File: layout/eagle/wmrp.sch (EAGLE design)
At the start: 131 parts, among them IC1 ACS712, IC2 ADR392, IC3 ATMEGA32U4TQFP-44, IC4 AD8552, IC5 AD8552, Q1 BC817-40, Q2 BC817-40, Q3 IRF7416, Q4 IRF7413, Q5 BC817-40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

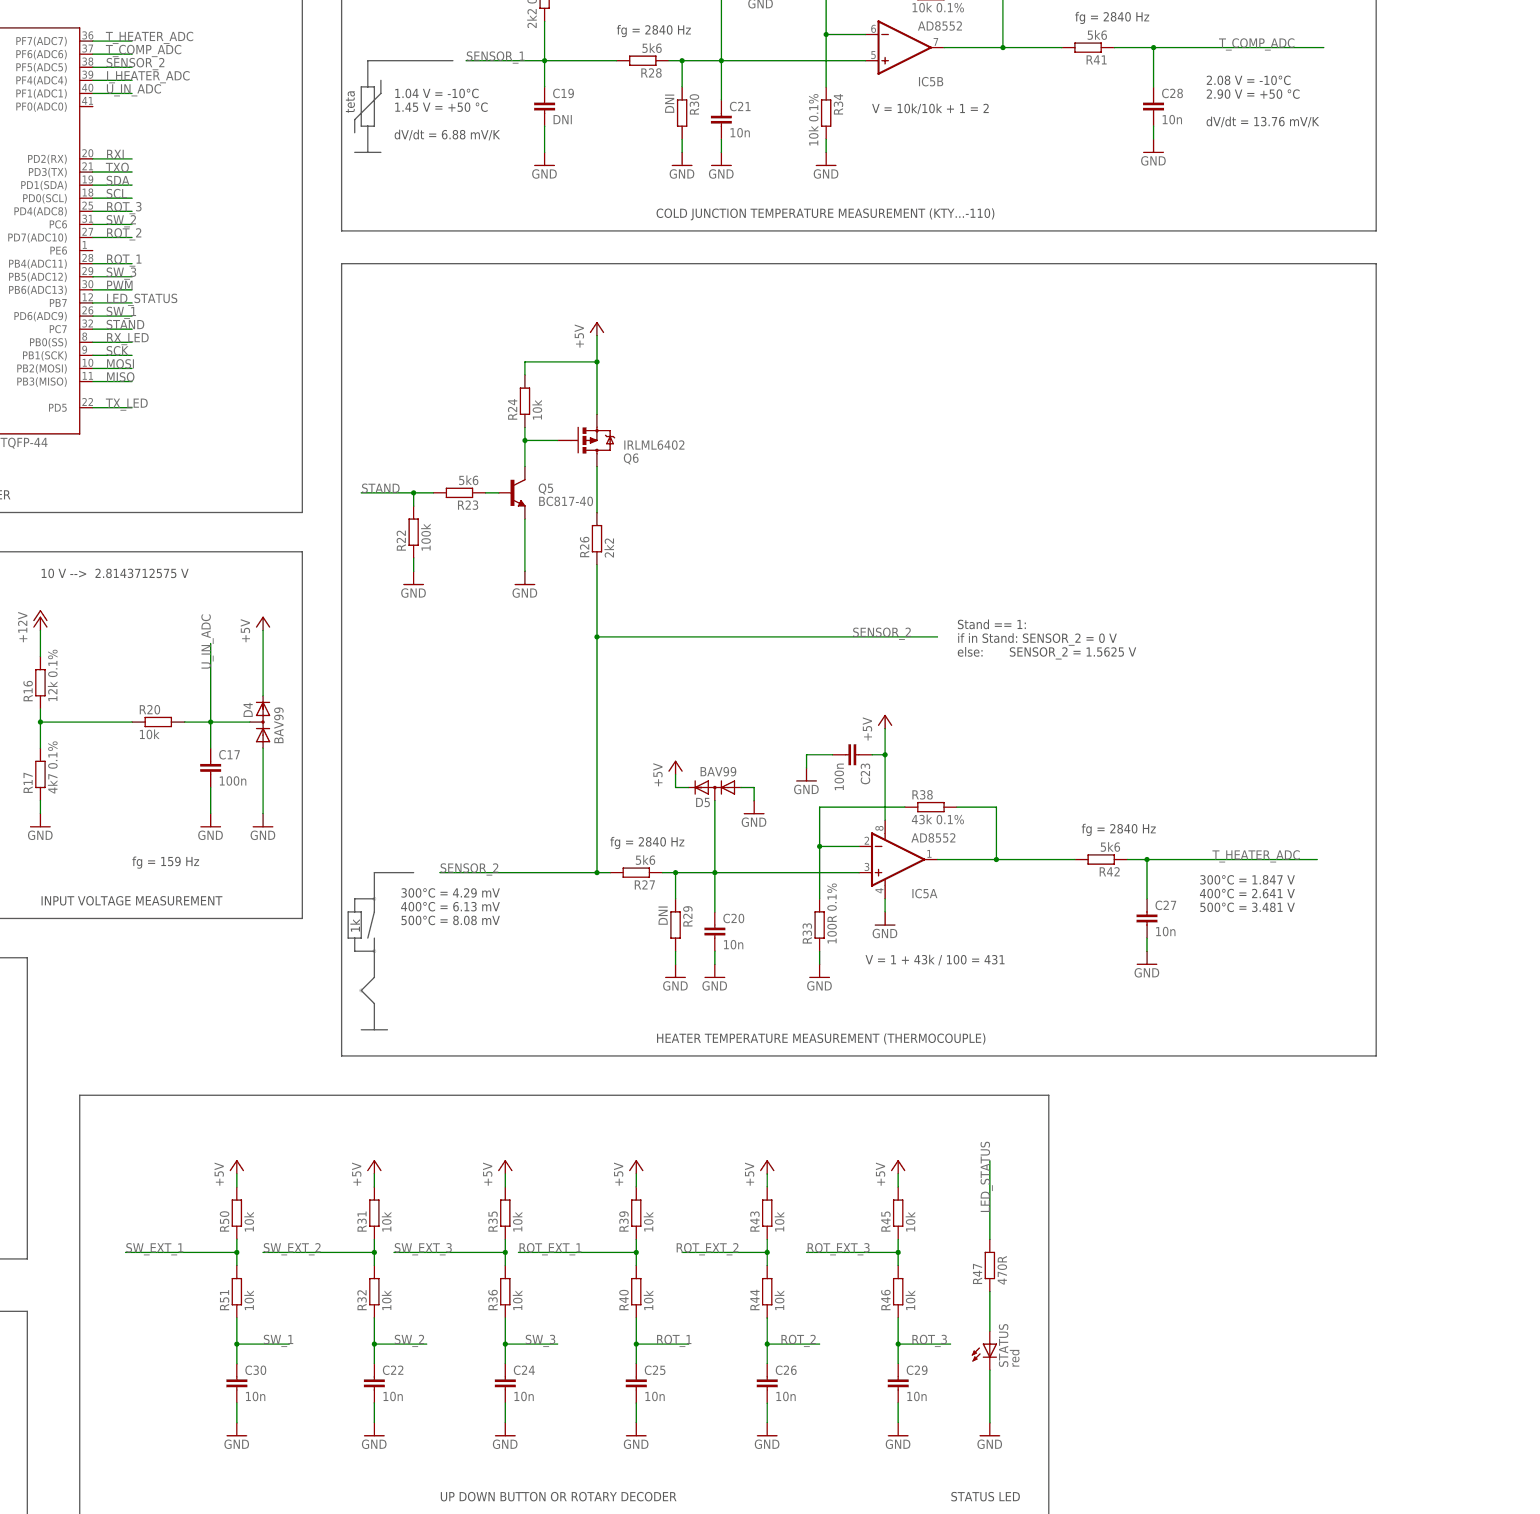
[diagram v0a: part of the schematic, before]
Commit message: Added SPI header and resistors to schematic, added SC and BL pin, moved RX_LED from pin 8 to 1
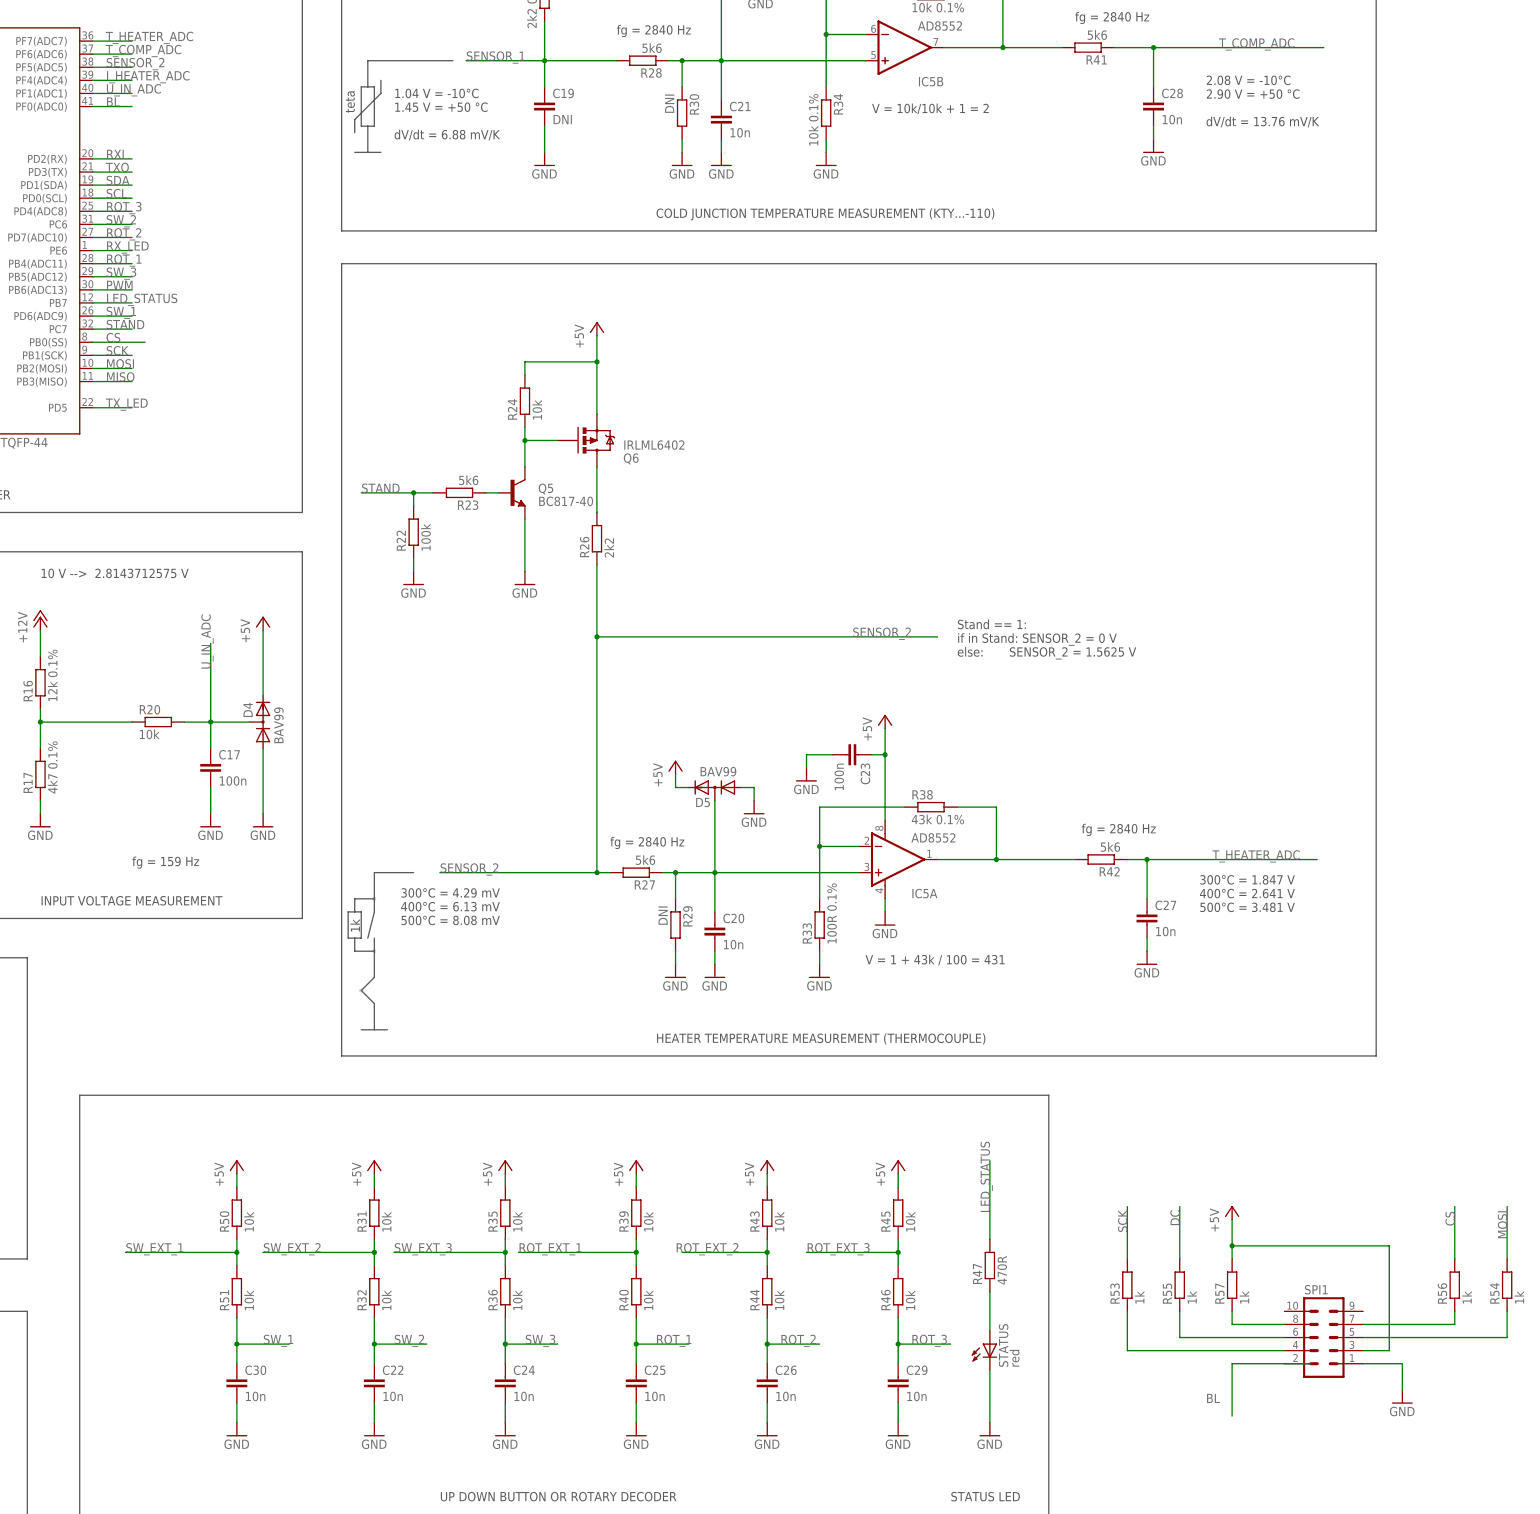
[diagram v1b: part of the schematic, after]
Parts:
- added R53, R54, R55, R56, R57: 1k, resistor:R-EU_R1206
- added SPI1: (no value), con-lstb:MA05-2
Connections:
- new net BL: IC3.PF0(ADC0), SPI1.2
- new net CS: IC3.PB0(SS), R56.2
- new net DC: R55.2
- new net N$35: R53.1, SPI1.4
- new net N$36: R54.1, SPI1.5
- new net N$37: R55.1, SPI1.6
- new net N$38: R56.1, SPI1.7
- new net N$40: R57.1, SPI1.8
- net +5V: now also R57.2, SPI1.3
- net GND: now also SPI1.1
- net MOSI: now also R54.2
- net RX_LED: now also IC3.PE6; no longer IC3.PB0(SS)
- net SCK: now also R53.2
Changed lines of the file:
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@@
 <?xml version="1.0" encoding="utf-8"?>
 <!DOCTYPE eagle SYSTEM "eagle.dtd">
-<eagle version="7.1.0">
+<eagle version="7.7.0">
 <drawing>
 <settings>
@@
 <setting verticaltext="up"/>
 </settings>
-<grid distance="0.1" unitdist="inch" unit="inch" style="lines" multiple="1" display="no" altdistance="0.01" altunitdist="inch" altunit="inch"/>
+<grid distance="0.1" unitdist="inch" unit="inch" style="lines" multiple="1" display="yes" altdistance="0.01" altunitdist="inch" altunit="inch"/>
 <layers>
 <layer number="1" name="Top" color="4" fill="1" visible="no" active="no"/>
@@
 <attribute name="REICHELT" value="MPE 087-2-010"/>
 </part>
+<part name="GND58" library="supply1" deviceset="GND" device=""/>
+<part name="P+33" library="supply1" deviceset="+5V" device=""/>
+<part name="SPI1" library="con-lstb" deviceset="MA05-2" device=""/>
+<part name="R53" library="resistor" deviceset="R-EU_" device="R1206" value="1k">
+<attribute name="REICHELT" value="-"/>
+</part>
+<part name="R54" library="resistor" deviceset="R-EU_" device="R1206" value="1k">
+<attribute name="REICHELT" value="-"/>
+</part>
+<part name="R55" library="resistor" deviceset="R-EU_" device="R1206" value="1k">
+<attribute name="REICHELT" value="-"/>
+</part>
+<part name="R56" library="resistor" deviceset="R-EU_" device="R1206" value="1k">
+<attribute name="REICHELT" value="-"/>
+</part>
+<part name="R57" library="resistor" deviceset="R-EU_" device="R1206" value="1k">
+<attribute name="REICHELT" value="-"/>
+</part>
 </parts>
 <sheets>
@@
 <attribute name="REICHELT" x="38.1" y="215.9" size="1.778" layer="96" display="off"/>
 </instance>
+<instance part="GND58" gate="1" x="434.34" y="-2.54"/>
+<instance part="P+33" gate="1" x="401.32" y="35.56"/>
+<instance part="SPI1" gate="G$1" x="419.1" y="10.16"/>
+<instance part="R53" gate="G$1" x="381" y="20.32" rot="R90">
+<attribute name="REICHELT" x="381" y="20.32" size="1.778" layer="96" rot="R90" display="off"/>
+</instance>
+<instance part="R54" gate="G$1" x="454.66" y="20.32" rot="R90">
+<attribute name="REICHELT" x="454.66" y="20.32" size="1.778" layer="96" rot="R90" display="off"/>
+</instance>
+<instance part="R55" gate="G$1" x="391.16" y="20.32" rot="R90">
+<attribute name="REICHELT" x="391.16" y="20.32" size="1.778" layer="96" rot="R90" display="off"/>
+</instance>
+<instance part="R56" gate="G$1" x="444.5" y="20.32" rot="R90">
+<attribute name="REICHELT" x="444.5" y="20.32" size="1.778" layer="96" rot="R90" display="off"/>
+</instance>
+<instance part="R57" gate="G$1" x="401.32" y="20.32" rot="R90">
+<attribute name="REICHELT" x="401.32" y="20.32" size="1.778" layer="96" rot="R90" display="off"/>
+</instance>
 </instances>
 <busses>
@@
 <wire x1="129.54" y1="269.24" x2="129.54" y2="270.51" width="0.1524" layer="91"/>
 </segment>
+<segment>
+<pinref part="SPI1" gate="G$1" pin="1"/>
+<pinref part="GND58" gate="1" pin="GND"/>
+<wire x1="426.72" y1="5.08" x2="434.34" y2="5.08" width="0.1524" layer="91"/>
+<wire x1="434.34" y1="5.08" x2="434.34" y2="0" width="0.1524" layer="91"/>
+</segment>
 </net>
 <net name="N$4" class="0">
@@
 <net name="RX_LED" class="0">
 <segment>
-<wire x1="180.34" y1="203.2" x2="187.96" y2="203.2" width="0.1524" layer="91"/>
-<label x="182.88" y="203.2" size="1.778" layer="95"/>
-<pinref part="IC3" gate="G$1" pin="PB0(SS)"/>
-</segment>
-<segment>
 <pinref part="RX_LEX" gate="G$1" pin="C"/>
 <wire x1="43.18" y1="39.37" x2="43.18" y2="31.75" width="0.1524" layer="91"/>
 <label x="43.18" y="31.75" size="1.778" layer="95"/>
 </segment>
+<segment>
+<pinref part="IC3" gate="G$1" pin="PE6"/>
+<wire x1="180.34" y1="220.98" x2="187.96" y2="220.98" width="0.1524" layer="91"/>
+<label x="182.88" y="220.98" size="1.778" layer="95"/>
+</segment>
 </net>
 <net name="SCK" class="0">
@@
 <pinref part="ISP" gate="A" pin="7"/>
 </segment>
+<segment>
+<pinref part="R53" gate="G$1" pin="2"/>
+<wire x1="381" y1="25.4" x2="381" y2="35.56" width="0.1524" layer="91"/>
+<label x="381" y="30.48" size="1.778" layer="95" rot="R90"/>
+</segment>
 </net>
 <net name="MOSI" class="0">
@@
 <pinref part="ISP" gate="A" pin="1"/>
 </segment>
+<segment>
+<pinref part="R54" gate="G$1" pin="2"/>
+<wire x1="454.66" y1="25.4" x2="454.66" y2="35.56" width="0.1524" layer="91"/>
+<label x="454.66" y="29.21" size="1.778" layer="95" rot="R90"/>
+</segment>
 </net>
 <net name="MISO" class="0">
@@
 <pinref part="R50" gate="G$1" pin="2"/>
 </segment>
+<segment>
+<pinref part="R57" gate="G$1" pin="2"/>
+<wire x1="401.32" y1="25.4" x2="401.32" y2="27.94" width="0.1524" layer="91"/>
+<pinref part="P+33" gate="1" pin="+5V"/>
+<wire x1="401.32" y1="27.94" x2="401.32" y2="33.02" width="0.1524" layer="91"/>
+<wire x1="401.32" y1="27.94" x2="431.8" y2="27.94" width="0.1524" layer="91"/>
+<wire x1="431.8" y1="27.94" x2="431.8" y2="7.62" width="0.1524" layer="91"/>
+<junction x="401.32" y="27.94"/>
+<pinref part="SPI1" gate="G$1" pin="3"/>
+<wire x1="431.8" y1="7.62" x2="426.72" y2="7.62" width="0.1524" layer="91"/>
+</segment>
 </net>
 <net name="UCAP" class="0">
@@
 </segment>
 </net>
+<net name="BL" class="0">
+<segment>
+<pinref part="SPI1" gate="G$1" pin="2"/>
+<wire x1="416.56" y1="5.08" x2="411.48" y2="5.08" width="0.1524" layer="91"/>
+<wire x1="411.48" y1="5.08" x2="401.32" y2="5.08" width="0.1524" layer="91"/>
+<wire x1="401.32" y1="5.08" x2="401.32" y2="-5.08" width="0.1524" layer="91"/>
+<label x="396.24" y="-2.54" size="1.778" layer="95"/>
+</segment>
+<segment>
+<pinref part="IC3" gate="G$1" pin="PF0(ADC0)"/>
+<wire x1="180.34" y1="248.92" x2="187.96" y2="248.92" width="0.1524" layer="91"/>
+<label x="182.88" y="248.92" size="1.778" layer="95"/>
+</segment>
+</net>
+<net name="N$35" class="0">
+<segment>
+<pinref part="R53" gate="G$1" pin="1"/>
+<wire x1="381" y1="15.24" x2="381" y2="7.62" width="0.1524" layer="91"/>
+<pinref part="SPI1" gate="G$1" pin="4"/>
+<wire x1="381" y1="7.62" x2="411.48" y2="7.62" width="0.1524" layer="91"/>
+</segment>
+</net>
+<net name="N$36" class="0">
+<segment>
+<pinref part="SPI1" gate="G$1" pin="5"/>
+<wire x1="426.72" y1="10.16" x2="454.66" y2="10.16" width="0.1524" layer="91"/>
+<pinref part="R54" gate="G$1" pin="1"/>
+<wire x1="454.66" y1="10.16" x2="454.66" y2="15.24" width="0.1524" layer="91"/>
+</segment>
+</net>
+<net name="N$37" class="0">
+<segment>
+<pinref part="SPI1" gate="G$1" pin="6"/>
+<wire x1="411.48" y1="10.16" x2="391.16" y2="10.16" width="0.1524" layer="91"/>
+<pinref part="R55" gate="G$1" pin="1"/>
+<wire x1="391.16" y1="10.16" x2="391.16" y2="15.24" width="0.1524" layer="91"/>
+</segment>
+</net>
+<net name="N$38" class="0">
+<segment>
+<pinref part="SPI1" gate="G$1" pin="7"/>
+<pinref part="R56" gate="G$1" pin="1"/>
+<wire x1="426.72" y1="12.7" x2="444.5" y2="12.7" width="0.1524" layer="91"/>
+<wire x1="444.5" y1="12.7" x2="444.5" y2="15.24" width="0.1524" layer="91"/>
+</segment>
+</net>
+<net name="N$40" class="0">
+<segment>
+<pinref part="SPI1" gate="G$1" pin="8"/>
+<pinref part="R57" gate="G$1" pin="1"/>
+<wire x1="411.48" y1="12.7" x2="401.32" y2="12.7" width="0.1524" layer="91"/>
+<wire x1="401.32" y1="12.7" x2="401.32" y2="15.24" width="0.1524" layer="91"/>
+</segment>
+</net>
+<net name="DC" class="0">
+<segment>
+<pinref part="R55" gate="G$1" pin="2"/>
+<wire x1="391.16" y1="25.4" x2="391.16" y2="35.56" width="0.1524" layer="91"/>
+<label x="391.16" y="31.75" size="1.778" layer="95" rot="R90"/>
+</segment>
+</net>
+<net name="CS" class="0">
+<segment>
+<pinref part="R56" gate="G$1" pin="2"/>
+<wire x1="444.5" y1="25.4" x2="444.5" y2="35.56" width="0.1524" layer="91"/>
+<label x="444.5" y="31.75" size="1.778" layer="95" rot="R90"/>
+</segment>
+<segment>
+<wire x1="180.34" y1="203.2" x2="190.5" y2="203.2" width="0.1524" layer="91"/>
+<label x="182.88" y="203.2" size="1.778" layer="95"/>
+<pinref part="IC3" gate="G$1" pin="PB0(SS)"/>
+</segment>
+</net>
 </nets>
 </sheet>
 </sheets>
+<errors>
+</errors>
 </schematic>
 </drawing>
